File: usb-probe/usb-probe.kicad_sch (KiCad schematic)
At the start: 5 parts, among them J1 USB_C_Receptacle, J2 Conn_02x09_Top_Bottom, J3 USB_C_Receptacle

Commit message: Started routing PCB
And fixed an accidental connection in the schema.
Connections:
- net RX2+: no longer J1.A3 (TX1-), J2.16 (Pin_16), J3.A3 (TX1-)
- new net TX1-: J1.A3 (TX1-), J2.16 (Pin_16), J3.A3 (TX1-)
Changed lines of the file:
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@@
   (junction (at 123.19 74.93) (diameter 0) (color 0 0 0 0)
   )
-  (junction (at 168.91 110.49) (diameter 0) (color 0 0 0 0)
-  )
   (junction (at 166.37 72.39) (diameter 0) (color 0 0 0 0)
   )
@@
     (stroke (width 0) (type default))
   )
-  (wire (pts (xy 168.91 110.49) (xy 176.53 110.49))
+  (wire (pts (xy 153.67 110.49) (xy 176.53 110.49))
     (stroke (width 0) (type default))
   )
@@
     (stroke (width 0) (type default))
   )
-  (wire (pts (xy 168.91 100.33) (xy 168.91 110.49))
-    (stroke (width 0) (type default))
-  )
   (wire (pts (xy 151.13 135.89) (xy 156.21 135.89))
     (stroke (width 0) (type default))
@@
     (stroke (width 0) (type default))
   )
-  (wire (pts (xy 168.91 110.49) (xy 168.91 148.59))
+  (wire (pts (xy 168.91 100.33) (xy 168.91 148.59))
     (stroke (width 0) (type default))
   )
@@
     (stroke (width 0) (type default))
   )
-  (wire (pts (xy 153.67 110.49) (xy 168.91 110.49))
-    (stroke (width 0) (type default))
-  )

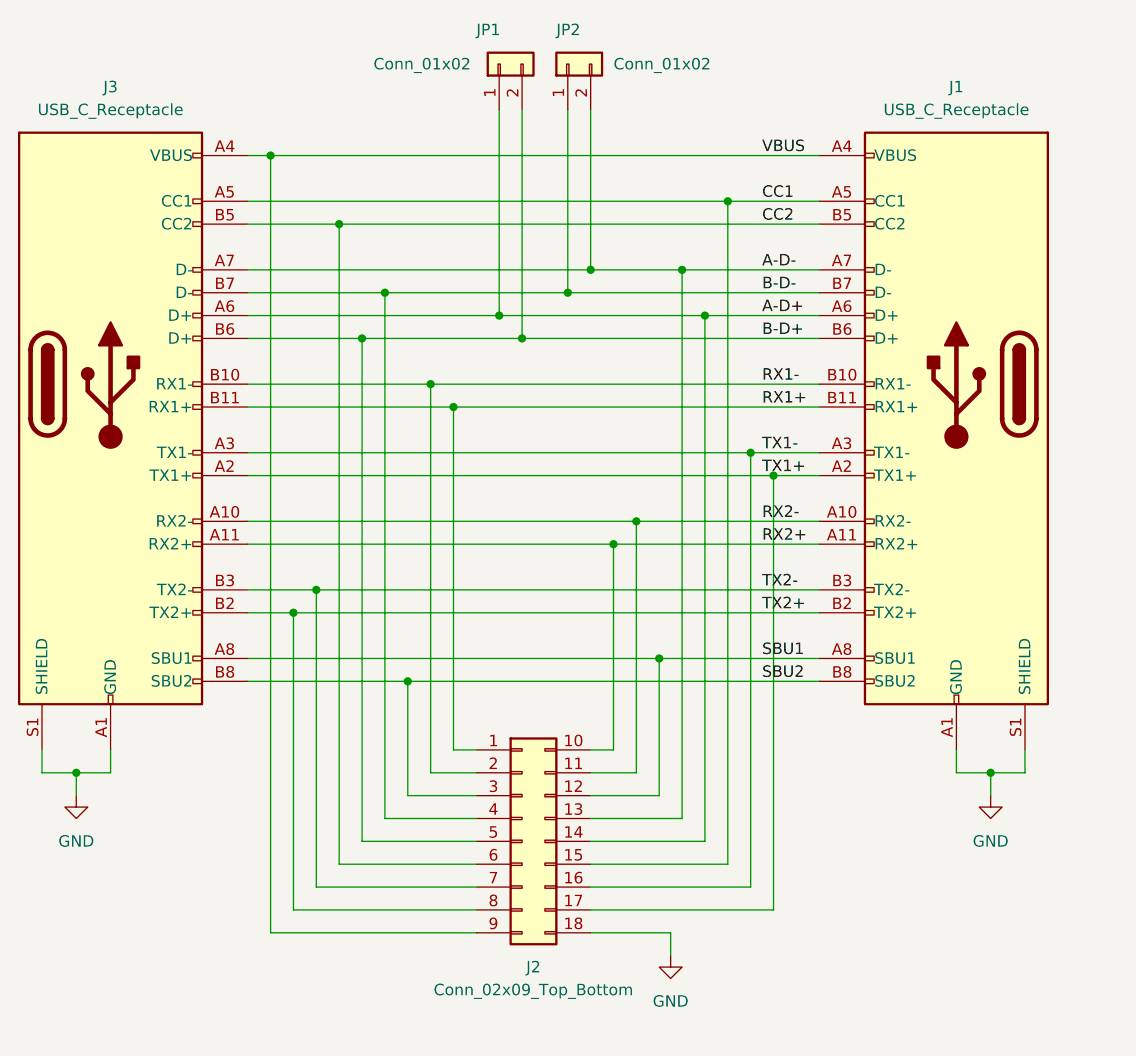
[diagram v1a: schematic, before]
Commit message: Routed B-side to pin header
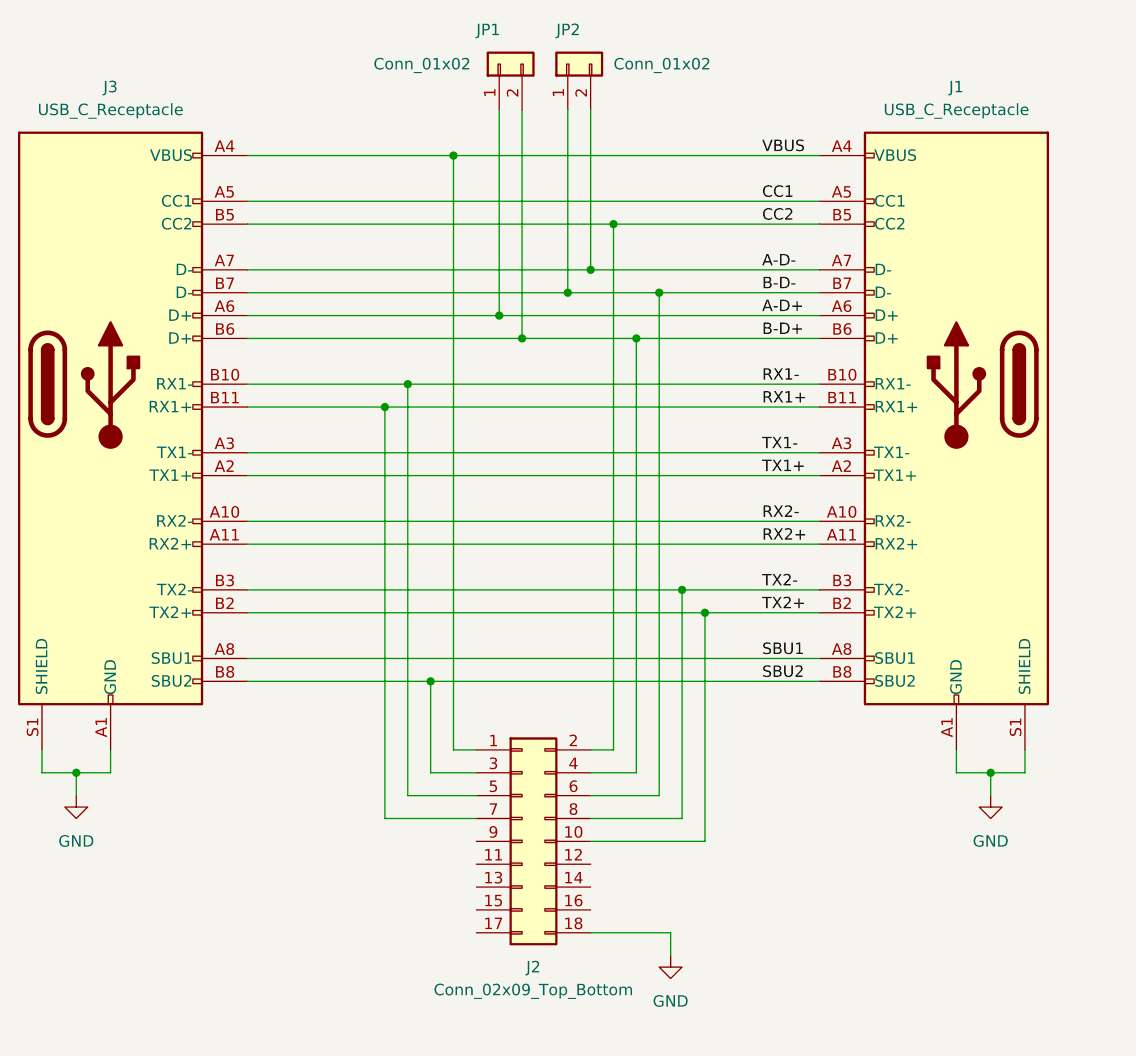
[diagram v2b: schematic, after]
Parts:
- J2: symbol Connector_Generic:Conn_02x09_Top_Bottom -> Connector_Generic:Conn_02x09_Odd_Even
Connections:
- net A-D+: no longer J2.14 (Pin_14)
- net A-D-: no longer J2.13 (Pin_13)
- net B-D+: now also J2.4 (Pin_4); no longer J2.5 (Pin_5)
- net B-D-: now also J2.6 (Pin_6); no longer J2.4 (Pin_4)
- net CC1: no longer J2.15 (Pin_15)
- net CC2: now also J2.2 (Pin_2); no longer J2.6 (Pin_6)
- net RX1+: now also J2.7 (Pin_7); no longer J2.1 (Pin_1)
- net RX1-: now also J2.5 (Pin_5); no longer J2.2 (Pin_2)
- net RX2+: no longer J2.10 (Pin_10)
- net RX2-: no longer J2.11 (Pin_11)
- net SBU1: no longer J2.12 (Pin_12)
- net TX1+: no longer J2.17 (Pin_17)
- net TX1-: no longer J2.16 (Pin_16)
- net TX2+: now also J2.10 (Pin_10); no longer J2.8 (Pin_8)
- net TX2-: now also J2.8 (Pin_8); no longer J2.7 (Pin_7)
- net VBUS: now also J2.1 (Pin_1); no longer J2.9 (Pin_9)

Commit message: Switched to USB-C Plug
I learned that USB-C cables have chips that encode their capabilities, so
putting two in series probably won't work. I've replaced one receptacle with a
plug.

I've also changed the pin header to an IDC connector, which should match what
my logic analyzer uses. By placing it between the USB-C plug and receptacle,
the routing becomes significantly simpler.
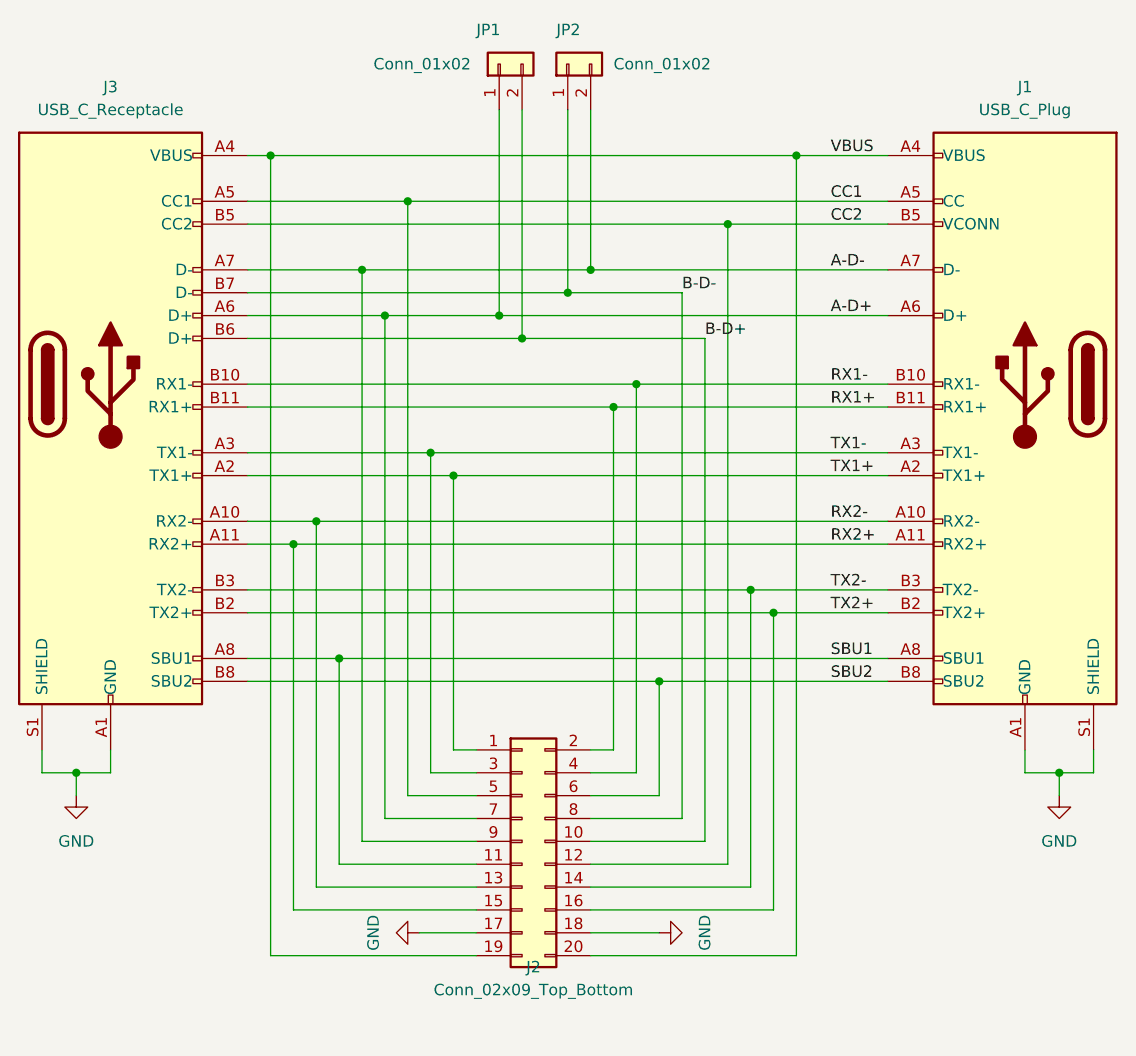
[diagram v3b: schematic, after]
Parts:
- J1: value USB_C_Receptacle -> USB_C_Plug; footprint Connector_USB:USB_C_Receptacle_Amphenol_12401610E4-2A -> Connector_USB:USB_C_Plug_Molex_105444; symbol Connector:USB_C_Receptacle -> Connector:USB_C_Plug
- J2: footprint Connector_PinHeader_2.54mm:PinHeader_2x09_P2.54mm_Vertical -> Connector_IDC:IDC-Header_2x10_P2.54mm_Vertical; symbol Connector_Generic:Conn_02x09_Odd_Even -> Connector_Generic:Conn_02x10_Odd_Even
- J3: footprint Connector_USB:USB_C_Receptacle_Amphenol_12401610E4-2A -> Connector_USB:USB_C_Receptacle_Molex_105450-0101
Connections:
- net A-D+: now also J2.7 (Pin_7)
- net A-D-: now also J2.9 (Pin_9)
- net B-D+: now also J2.10 (Pin_10); no longer J1.B6 (D+), J2.4 (Pin_4)
- net B-D-: now also J2.8 (Pin_8); no longer J1.B7 (D-), J2.6 (Pin_6)
- net CC1: now also J2.5 (Pin_5)
- net CC2: now also J2.12 (Pin_12); no longer J2.2 (Pin_2)
- net GND: now also J2.17 (Pin_17)
- net RX1+: now also J2.2 (Pin_2); no longer J2.7 (Pin_7)
- net RX1-: now also J2.4 (Pin_4); no longer J2.5 (Pin_5)
- net RX2+: now also J2.15 (Pin_15)
- net RX2-: now also J2.13 (Pin_13)
- net SBU1: now also J2.11 (Pin_11)
- net SBU2: now also J2.6 (Pin_6); no longer J2.3 (Pin_3)
- net TX1+: now also J2.1 (Pin_1)
- net TX1-: now also J2.3 (Pin_3)
- net TX2+: now also J2.16 (Pin_16); no longer J2.10 (Pin_10)
- net TX2-: now also J2.14 (Pin_14); no longer J2.8 (Pin_8)
- net VBUS: now also J2.19 (Pin_19), J2.20 (Pin_20); no longer J2.1 (Pin_1)

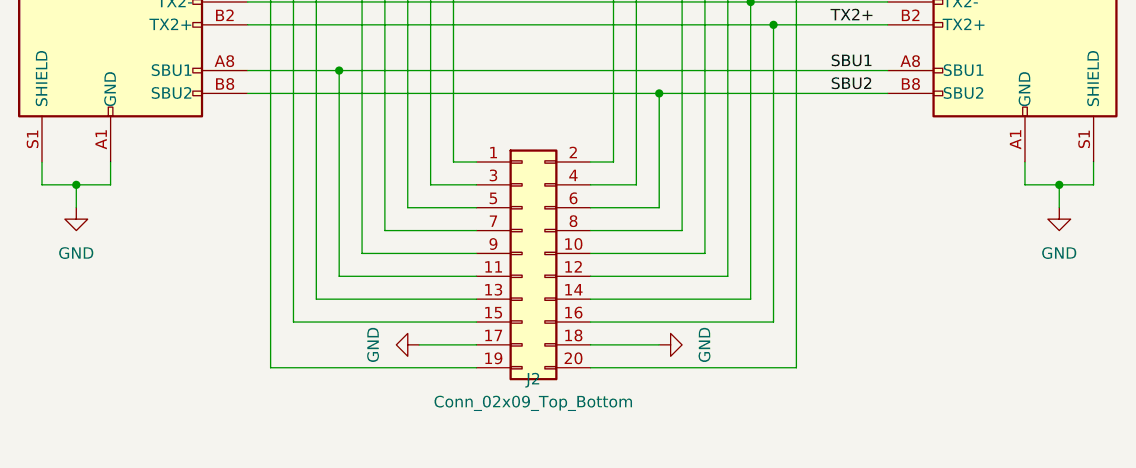
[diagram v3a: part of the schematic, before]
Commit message: Disconnect Ground and Shield
It's up to the connected device to decide what to do with the shield, we just
need to pass it through.

Fixes #4
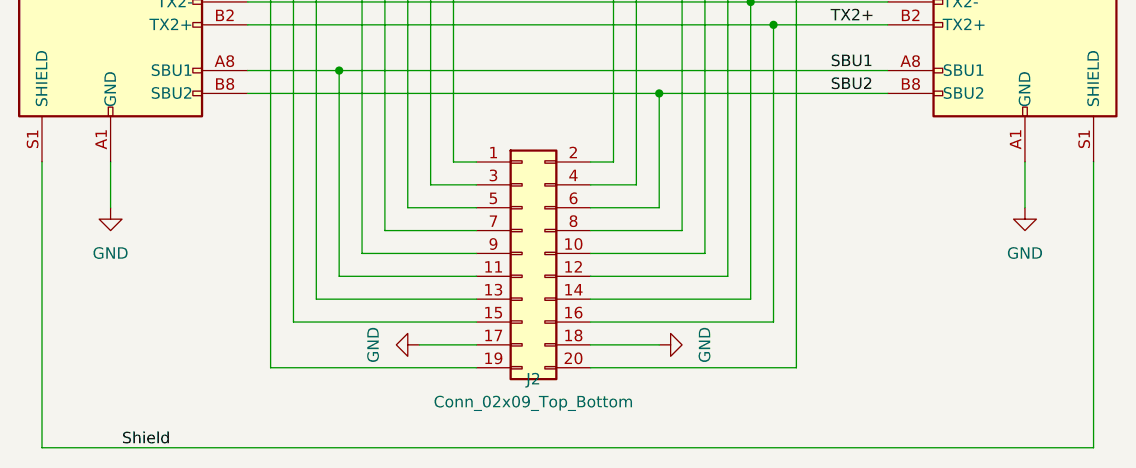
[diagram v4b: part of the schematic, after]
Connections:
- net GND: no longer J1.S1 (SHIELD), J3.S1 (SHIELD)
- new net Shield: J1.S1 (SHIELD), J3.S1 (SHIELD)
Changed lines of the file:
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@@
   (junction (at 140.97 85.09) (diameter 0) (color 0 0 0 0)
   )
-  (junction (at 93.98 135.89) (diameter 0) (color 0 0 0 0)
-  )
   (junction (at 166.37 74.93) (diameter 0) (color 0 0 0 0)
   )
@@
   (junction (at 168.91 115.57) (diameter 0) (color 0 0 0 0)
   )
-  (junction (at 203.2 135.89) (diameter 0) (color 0 0 0 0)
-  )
   (junction (at 115.57 67.31) (diameter 0) (color 0 0 0 0)
   )
@@
     (stroke (width 0) (type default))
   )
-  (wire (pts (xy 207.01 133.35) (xy 207.01 135.89))
-    (stroke (width 0) (type default))
-  )
   (wire (pts (xy 143.51 62.23) (xy 143.51 87.63))
     (stroke (width 0) (type default))
@@
     (stroke (width 0) (type default))
   )
+  (wire (pts (xy 90.17 165.1) (xy 207.01 165.1))
+    (stroke (width 0) (type default))
+  )
   (wire (pts (xy 113.03 67.31) (xy 115.57 67.31))
     (stroke (width 0) (type default))
@@
     (stroke (width 0) (type default))
   )
-  (wire (pts (xy 97.79 135.89) (xy 93.98 135.89))
-    (stroke (width 0) (type default))
-  )
   (wire (pts (xy 163.83 143.51) (xy 163.83 87.63))
     (stroke (width 0) (type default))
@@
     (stroke (width 0) (type default))
   )
-  (wire (pts (xy 207.01 135.89) (xy 203.2 135.89))
-    (stroke (width 0) (type default))
-  )
   (wire (pts (xy 156.21 92.71) (xy 184.15 92.71))
     (stroke (width 0) (type default))
@@
     (stroke (width 0) (type default))
   )
-  (wire (pts (xy 90.17 135.89) (xy 93.98 135.89))
-    (stroke (width 0) (type default))
-  )
   (wire (pts (xy 168.91 115.57) (xy 184.15 115.57))
     (stroke (width 0) (type default))
@@
     (stroke (width 0) (type default))
   )
-  (wire (pts (xy 90.17 133.35) (xy 90.17 135.89))
+  (wire (pts (xy 90.17 133.35) (xy 90.17 165.1))
     (stroke (width 0) (type default))
   )
@@
     (stroke (width 0) (type default))
   )
-  (wire (pts (xy 93.98 135.89) (xy 93.98 138.43))
-    (stroke (width 0) (type default))
-  )
   (wire (pts (xy 168.91 148.59) (xy 168.91 115.57))
     (stroke (width 0) (type default))
@@
     (stroke (width 0) (type default))
   )
-  (wire (pts (xy 203.2 135.89) (xy 203.2 138.43))
-    (stroke (width 0) (type default))
-  )
   (wire (pts (xy 113.03 92.71) (xy 156.21 92.71))
     (stroke (width 0) (type default))
@@
     (stroke (width 0) (type default))
   )
-  (wire (pts (xy 97.79 133.35) (xy 97.79 135.89))
+  (wire (pts (xy 97.79 133.35) (xy 97.79 138.43))
     (stroke (width 0) (type default))
   )
@@
     (stroke (width 0) (type default))
   )
-  (wire (pts (xy 199.39 133.35) (xy 199.39 135.89))
+  (wire (pts (xy 199.39 133.35) (xy 199.39 138.43))
+    (stroke (width 0) (type default))
+  )
+  (wire (pts (xy 207.01 133.35) (xy 207.01 165.1))
     (stroke (width 0) (type default))
   )
@@
     (stroke (width 0) (type default))
   )
-  (wire (pts (xy 199.39 135.89) (xy 203.2 135.89))
-    (stroke (width 0) (type default))
-  )
   (wire (pts (xy 171.45 118.11) (xy 184.15 118.11))
     (stroke (width 0) (type default))
@@
   )
   (label "RX2+" (at 177.8 110.49 0) (fields_autoplaced)
+    (effects (font (size 1.27 1.27)) (justify left bottom))
+  )
+  (label "Shield" (at 99.06 165.1 0) (fields_autoplaced)
     (effects (font (size 1.27 1.27)) (justify left bottom))
   )
@@
     )
   )
-  (symbol (lib_id "power:GND") (at 93.98 138.43 0) (unit 1)
+  (symbol (lib_id "power:GND") (at 97.79 138.43 0) (unit 1)
     (in_bom yes) (on_board yes) (dnp no) (fields_autoplaced)
-    (property "Reference" "#PWR02" (at 93.98 144.78 0)
-      (effects (font (size 1.27 1.27)) hide)
-    )
-    (property "Value" "GND" (at 93.98 143.51 0)
-      (effects (font (size 1.27 1.27)))
-    )
-    (property "Footprint" "" (at 93.98 138.43 0)
-      (effects (font (size 1.27 1.27)) hide)
-    )
-    (property "Datasheet" "" (at 93.98 138.43 0)
+    (property "Reference" "#PWR02" (at 97.79 144.78 0)
+      (effects (font (size 1.27 1.27)) hide)
+    )
+    (property "Value" "GND" (at 97.79 143.51 0)
+      (effects (font (size 1.27 1.27)))
+    )
+    (property "Footprint" "" (at 97.79 138.43 0)
+      (effects (font (size 1.27 1.27)) hide)
+    )
+    (property "Datasheet" "" (at 97.79 138.43 0)
       (effects (font (size 1.27 1.27)) hide)
     )
@@
     )
   )
-  (symbol (lib_id "power:GND") (at 203.2 138.43 0) (unit 1)
+  (symbol (lib_id "power:GND") (at 199.39 138.43 0) (unit 1)
     (in_bom yes) (on_board yes) (dnp no) (fields_autoplaced)
-    (property "Reference" "#PWR01" (at 203.2 144.78 0)
-      (effects (font (size 1.27 1.27)) hide)
-    )
-    (property "Value" "GND" (at 203.2 143.51 0)
-      (effects (font (size 1.27 1.27)))
-    )
-    (property "Footprint" "" (at 203.2 138.43 0)
-      (effects (font (size 1.27 1.27)) hide)
-    )
-    (property "Datasheet" "" (at 203.2 138.43 0)
-      (effects (font (size 1.27 1.27)) hide)
-    )
+    (property "Reference" "#PWR01" (at 199.39 144.78 0)
+      (effects (font (size 1.27 1.27)) hide)
+    )
+    (property "Value" "GND" (at 199.39 143.51 0)
+      (effects (font (size 1.27 1.27)))
+    )
+    (property "Footprint" "" (at 199.39 138.43 0)
+      (effects (font (size 1.27 1.27)) hide)
+    )
+    (property "Datasheet" "" (at 199.39 138.43 0)
+      (effects (font (size 1.27 1.27)) hide)
+    )
